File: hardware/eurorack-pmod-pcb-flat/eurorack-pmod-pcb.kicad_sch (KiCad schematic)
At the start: 28 parts, among them J1 PMOD, J2 EURORACK_PWR, U1 LM1117-3.3, U2 TL072, U3 AK4619VN

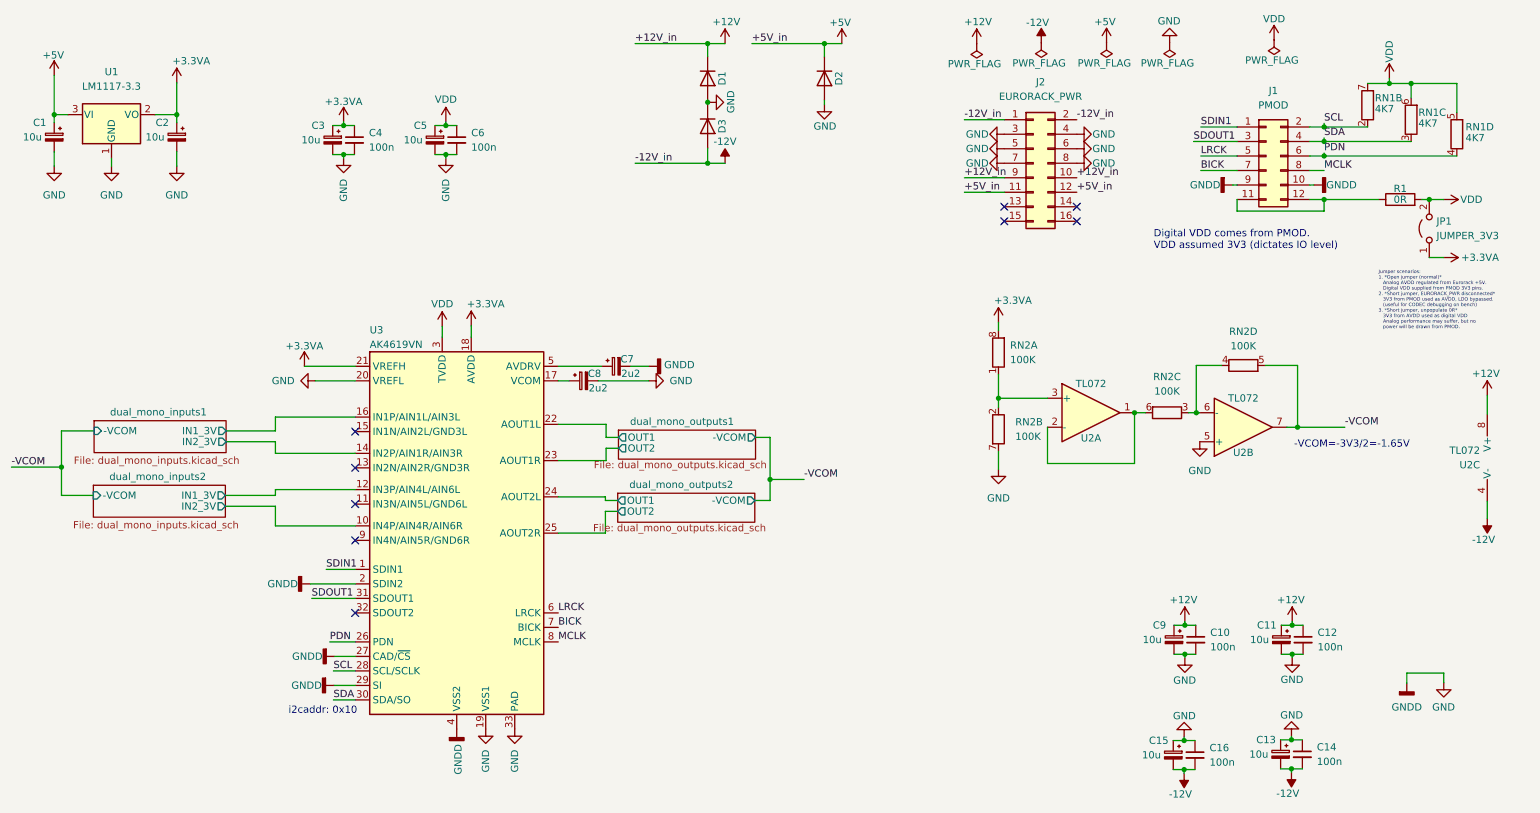
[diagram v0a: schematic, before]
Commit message: rev2-flat: add vref and stabilization caps
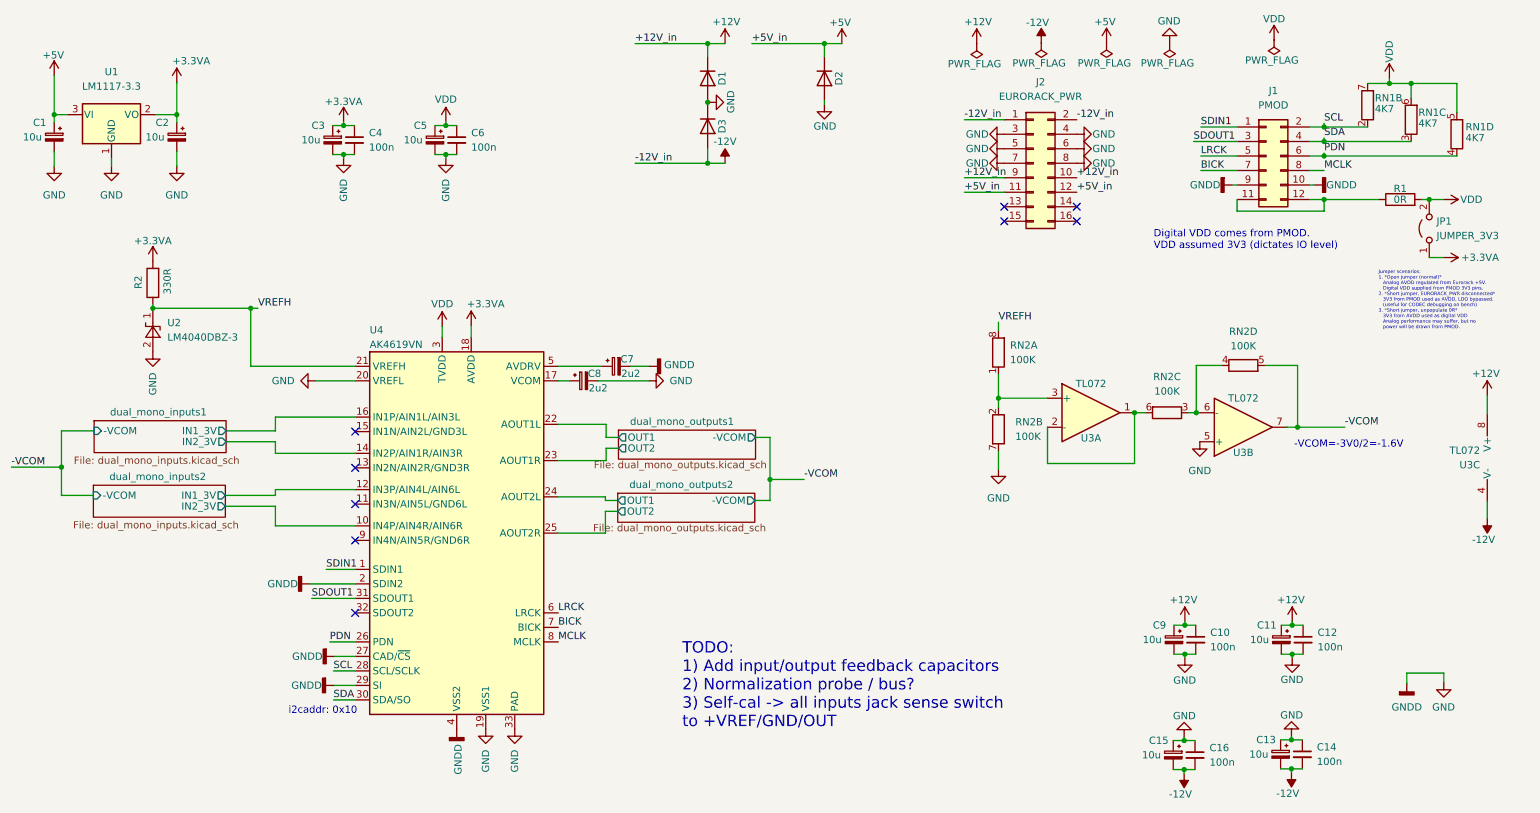
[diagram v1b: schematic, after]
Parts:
- added R2: 330R, Resistor_SMD:R_0603_1608Metric, symbol Device:R
- added U2: LM4040DBZ-3, Package_TO_SOT_SMD:SOT-23, symbol Reference_Voltage:LM4040DBZ-3
- renumbered U2 to U3, U3 to U4
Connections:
- net +3.3VA: now also R2.2; no longer RN2.8 (R1.2), U4.21 (VREFH)
- net GND: now also U2.2 (A)
- new net VREFH: R2.1, RN2.8 (R1.2), U2.1 (K), U4.21 (VREFH)
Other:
- note added: "-VCOM=-3V0/2=-1.6V"
- note added: "TODO: 1) Add input/output feedback capacitors 2) Normalization probe / bus? 3) Self-cal -> all inputs jack sense switch to +VREF/GND/OUT"
- note removed: "-VCOM=-3V3/2=-1.65V"

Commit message: rev2-flat: update power supply and add bypass electros
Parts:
- removed D2: 1N4007FL, Diode_SMD:D_SOD-123F, symbol Diode:US1G
- removed J2: EURORACK_PWR, Connector_PinHeader_2.54mm:PinHeader_2x08_P2.54mm_Vertical, symbol Connector_Generic:Conn_02x08_Odd_Even
- removed JP1: JUMPER_3V3, Connector_PinHeader_2.54mm:PinHeader_1x02_P2.54mm_Vertical, symbol Jumper:Jumper_2_Open
- removed R1: 0R, Resistor_SMD:R_0603_1608Metric, symbol Device:R
- removed U1: LM1117-3.3, Package_TO_SOT_SMD:SOT-223-3_TabPin2, symbol Regulator_Linear:LM1117-3.3
- added C7: 47u, Capacitor_SMD:CP_Elec_5x5.3, symbol Device:C_Polarized_Small
- added C8: 10u, Capacitor_Tantalum_SMD:CP_EIA-3216-10_Kemet-I, symbol Device:C_Polarized_Small
- added C9: 100n, Capacitor_SMD:C_0603_1608Metric, symbol Device:C_Small
- added J1: EURORACK_PWR, Connector_PinHeader_2.54mm:PinHeader_2x05_P2.54mm_Vertical, symbol Connector_Generic:Conn_02x05_Odd_Even
- added L1, L2, L3, L4: Ferrite, Inductor_SMD:L_0603_1608Metric, symbol Device:L_Ferrite_Small
- C1, C2: value 10u -> 47u; footprint Capacitor_Tantalum_SMD:CP_EIA-3216-10_Kemet-I -> Capacitor_SMD:CP_Elec_5x5.3; dig# 399-18019-1-ND -> 493-14540-1-ND; mfg# T491A106K020AT -> UCM1V470MCL1GS
- renumbered C7 to C10, C8 to C11, C9 to C12, C10 to C13, C11 to C14, C12 to C15, C13 to C16, C14 to C17, C15 to C18, C16 to C19, D3 to D2, J1 to J2, R2 to R1, U2 to U1, U3 to U2, U4 to U3
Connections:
- net +12V: now also C1.1, L1.1; no longer D1.1 (K)
- net +3.3VA: now also L4.1; no longer C2.1
- net +5V: no longer C1.1
- net -12V: now also C2.2, L2.1; no longer D2.2 (A)
- net GND: now also C2.1, C7.2, C8.2, C9.2, J1.3 (Pin_3), J1.4 (Pin_4), J1.5 (Pin_5), J1.6 (Pin_6), J1.7 (Pin_7), J1.8 (Pin_8); no longer C2.2, D1.2 (A), D2.1 (K)
- net VDD: now also C7.1, L3.1, L4.2
- net VREFH: now also C8.1, C9.1
- net at J2.11 (Pin_11), J2.12 (Pin_12): now also L3.2
- new net: D1.1 (K), L1.2
- new net: D1.2 (A), J1.10 (Pin_10), J1.9 (Pin_9)
- new net: D2.1 (K), J1.1 (Pin_1), J1.2 (Pin_2)
- new net: D2.2 (A), L2.2
- no-connect marks 9 -> 5
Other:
- note added: "3V3 comes from PMOD"
- note removed: "Digital VDD comes from PMOD. VDD assumed 3V3 (dictates IO level)"
- note removed: "Jumper scenarios: 1. *Open jumper (normal)* Analog AVDD regulated from Eurorack +5V. Digital VDD supplied from PMOD 3V3 pins. 2. *Short jumper, EURORACK_PWR disconnected* 3V3 from PMOD used as AVDD, LDO bypassed. (useful for CODEC debugging on bench) 3. *Short jumper, unpopulate 0R* 3V3 from AVDD used as digital VDD Analog performance may suffer, but no power will be drawn from PMOD."
- moved on the sheet: D1, D2

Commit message: rev2-flat: update fields and fab1 export
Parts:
- RN1: dig# (none) -> CAT16-4701F4LFCT-ND; mfg# (none) -> CAT16-472F4LF
- RN2: dig# CAY16-1003F4LFCT-ND -> CAT16-1003F4LFCT-ND; mfg# CAY16-1003F4LF -> CAT16-1003F4LF
- U1: dig# (none) -> 296-LM4040CEM3X-3.0/NOPBCT-ND; mfg# (none) -> LM4040CEM3X-3.0/NOPB
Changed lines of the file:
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@@
+      (effects (font (size 1.27 1.27)) hide)
+    )
+    (property "dig#" "CAT16-4701F4LFCT-ND" (id 4) (at 259.715 33.02 0)
+      (effects (font (size 1.27 1.27)) hide)
+    )
+    (property "mfg#" "CAT16-472F4LF" (id 5) (at 259.715 33.02 0)
       (effects (font (size 1.27 1.27)) hide)
     )
@@
       (effects (font (size 1.27 1.27) italic) hide)
     )
+    (property "dig#" "296-LM4040CEM3X-3.0/NOPBCT-ND" (id 4) (at 46.99 72.39 0)
+      (effects (font (size 1.27 1.27)) hide)
+    )
+    (property "mfg#" "LM4040CEM3X-3.0/NOPB" (id 5) (at 46.99 72.39 0)
+      (effects (font (size 1.27 1.27)) hide)
+    )
     (pin "1")
     (pin "2")
@@
     )
     (property "Datasheet" "~" (id 3) (at 275.336 38.1 0)
+      (effects (font (size 1.27 1.27)) hide)
+    )
+    (property "dig#" "CAT16-4701F4LFCT-ND" (id 4) (at 275.336 38.1 0)
+      (effects (font (size 1.27 1.27)) hide)
+    )
+    (property "mfg#" "CAT16-472F4LF" (id 5) (at 275.336 38.1 0)
       (effects (font (size 1.27 1.27)) hide)
     )
@@
     )
     (property "Datasheet" "~" (id 3) (at 267.335 35.56 0)
+      (effects (font (size 1.27 1.27)) hide)
+    )
+    (property "dig#" "CAT16-4701F4LFCT-ND" (id 4) (at 267.335 35.56 0)
+      (effects (font (size 1.27 1.27)) hide)
+    )
+    (property "mfg#" "CAT16-472F4LF" (id 5) (at 267.335 35.56 0)
       (effects (font (size 1.27 1.27)) hide)
     )
@@
       (effects (font (size 1.27 1.27)) hide)
     )
-    (property "dig#" "CAY16-1003F4LFCT-ND" (id 4) (at 224.5868 90.7288 90)
-      (effects (font (size 1.27 1.27)) hide)
-    )
-    (property "mfg#" "CAY16-1003F4LF" (id 5) (at 224.5868 93.2688 90)
+    (property "dig#" "CAT16-1003F4LFCT-ND" (id 4) (at 224.5868 90.7288 90)
+      (effects (font (size 1.27 1.27)) hide)
+    )
+    (property "mfg#" "CAT16-1003F4LF" (id 5) (at 224.5868 93.2688 90)
       (effects (font (size 1.27 1.27)) hide)
     )
@@
       (effects (font (size 1.27 1.27)) hide)
     )
-    (property "dig#" "CAY16-1003F4LFCT-ND" (id 4) (at 197.104 85.2169 0)
+    (property "dig#" "CAT16-1003F4LFCT-ND" (id 4) (at 197.104 85.2169 0)
       (effects (font (size 1.27 1.27)) (justify left) hide)
     )
-    (property "mfg#" "CAY16-1003F4LF" (id 5) (at 197.104 87.7569 0)
+    (property "mfg#" "CAT16-1003F4LF" (id 5) (at 197.104 87.7569 0)
       (effects (font (size 1.27 1.27)) (justify left) hide)
     )
@@
       (effects (font (size 1.27 1.27)) hide)
     )
-    (property "dig#" "CAY16-1003F4LFCT-ND" (id 4) (at 198.0184 98.6535 0)
+    (property "dig#" "CAT16-1003F4LFCT-ND" (id 4) (at 198.0184 98.6535 0)
       (effects (font (size 1.27 1.27)) (justify right) hide)
     )
-    (property "mfg#" "CAY16-1003F4LF" (id 5) (at 198.0184 101.1935 0)
+    (property "mfg#" "CAT16-1003F4LF" (id 5) (at 198.0184 101.1935 0)
       (effects (font (size 1.27 1.27)) (justify right) hide)
     )
@@
       (effects (font (size 1.27 1.27)) hide)
     )
-    (property "dig#" "CAY16-1003F4LFCT-ND" (id 4) (at 237.9472 82.804 90)
-      (effects (font (size 1.27 1.27)) hide)
-    )
-    (property "mfg#" "CAY16-1003F4LF" (id 5) (at 237.9472 85.344 90)
-      (effects (font (size 1.27 1.27)) hide)
-    )
+    (property "dig#" "CAT16-1003F4LFCT-ND" (id 4) (at 237.9472 82.804 90)
+      (effects (font (size 1.27 1.27)) hide)
+    )
+    (property "mfg#" "CAT16-1003F4LF" (id 5) (at 237.9472 85.344 90)
+      (effects (font (size 1.27 1.27)) hide)
+    )
